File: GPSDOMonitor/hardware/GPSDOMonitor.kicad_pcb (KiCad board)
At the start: 2 copper layers, 4 parts, among them U1 PIC18LF2550-ISO, X1 ABM8W-20.0000MHZ-4-K1Z-T3

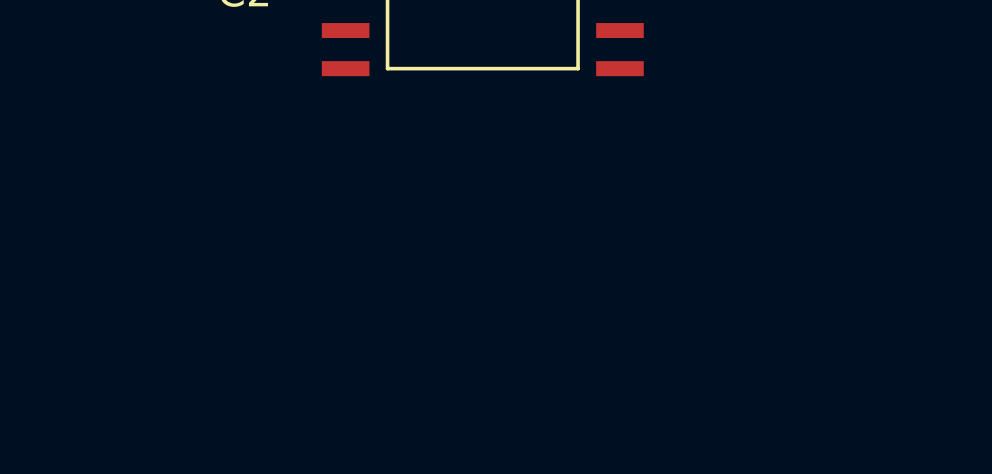
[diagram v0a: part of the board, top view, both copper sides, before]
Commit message: Add connector for the GPSDO
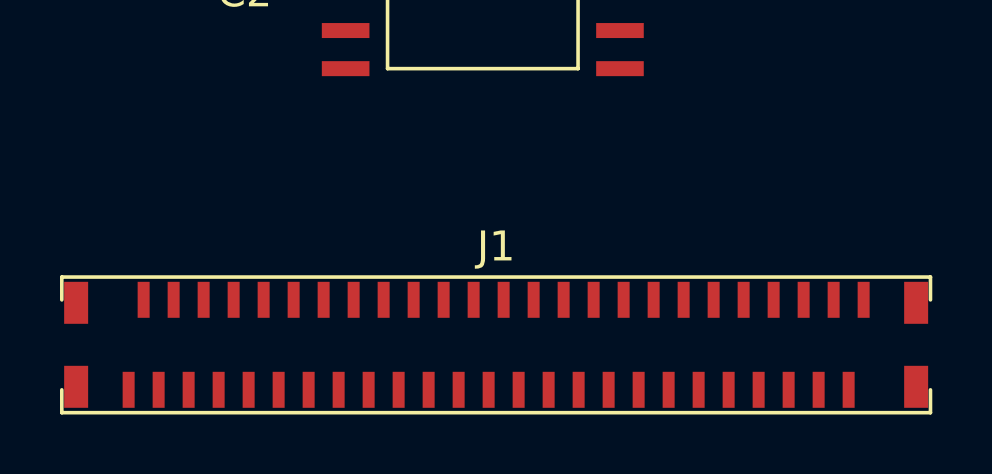
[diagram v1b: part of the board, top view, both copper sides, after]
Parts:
- added J1: F31S-1A7L1-11050, Connector_Data:F31S-1A7L1-11050, F.Cu at (96.1, 94.7)

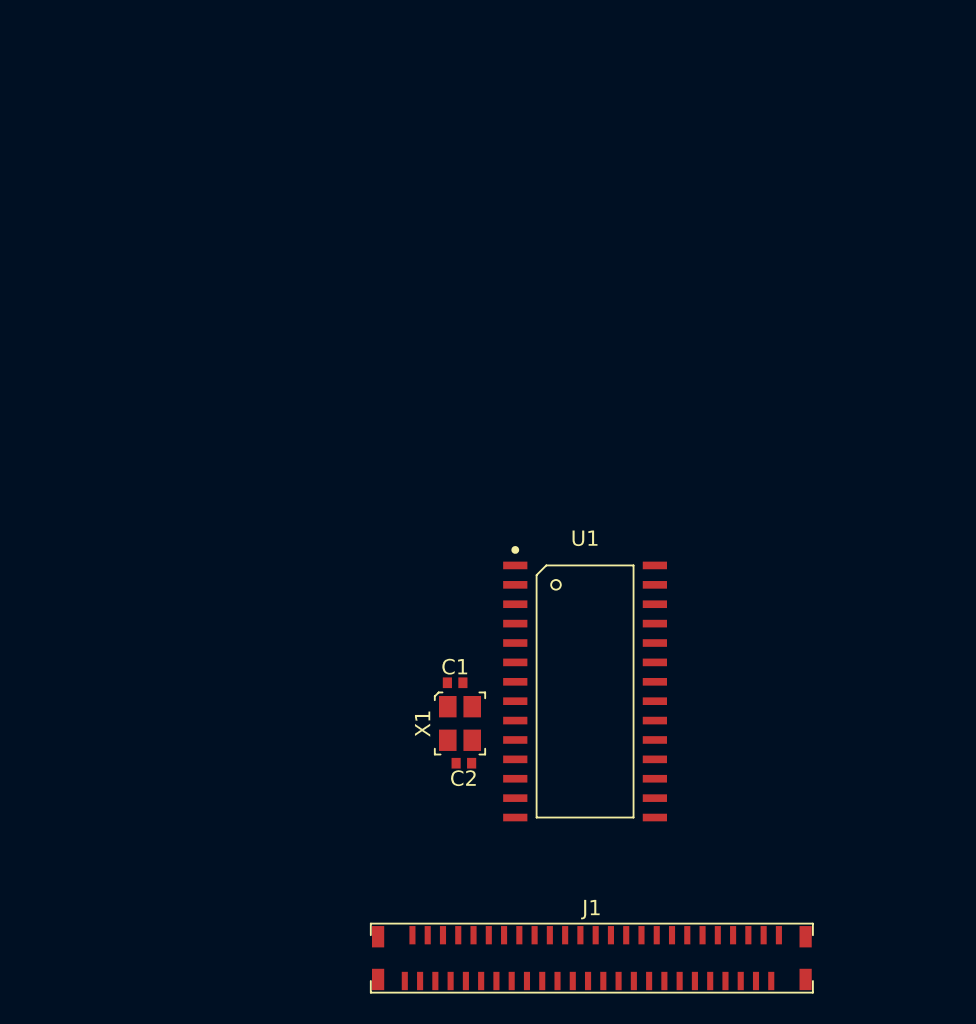
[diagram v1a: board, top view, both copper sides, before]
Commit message: Add 5.5v regulator schematic
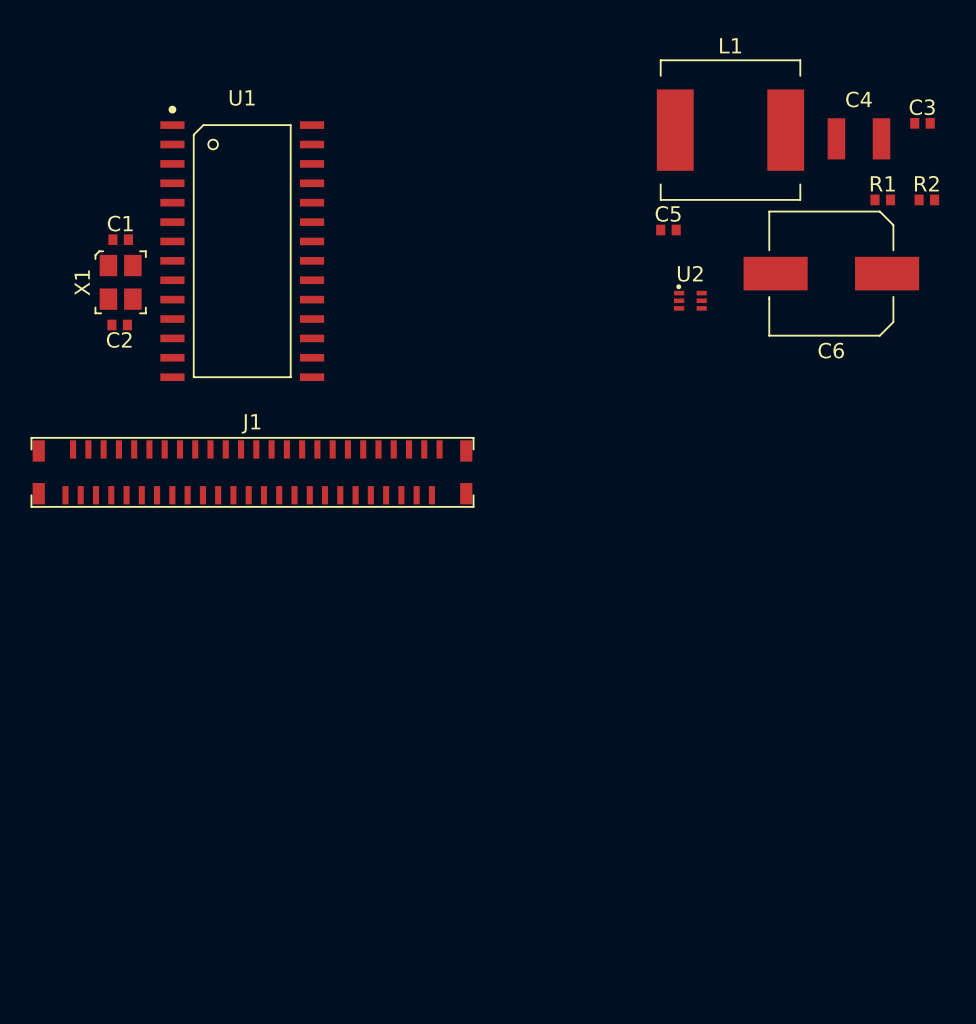
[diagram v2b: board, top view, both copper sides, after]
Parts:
- added C3: UMK105B7104KV-FR, Capacitor_Ceramic:C_0402_1005Metric, F.Cu at (117.7, 42.9)
- added C4: UMK325AB7106KM-P, Capacitor_Ceramic:C_1210_3225Metric, F.Cu at (113.6, 43.9)
- added C5: UMK105B7104KV-FR, Capacitor_Ceramic:C_0402_1005Metric, F.Cu at (101.1, 49.9)
- added C6: A768KE686M1GLAE038, Capacitor_Electrolytic:CP_Elec_KEMET_8mm, F.Cu at (111.8, 52.8)
- added L1: 74437356047, Inductor:74437356047, F.Cu at (105.2, 43.4)
- added R1: CRGCQ0402F82K, Resistor:R_0402_1005Metric, F.Cu at (115.1, 47.9)
- added R2: CRGCQ0402F10K, Resistor:R_0402_1005Metric, F.Cu at (118.0, 47.9)
- added U2: TPS563231DRLR, Package_TO_SOT:SOT-563, F.Cu at (102.5, 54.5)
- moved J1 38.8 mm to (73.9, 62.9)
- moved U1 36.5 mm to (73.2, 51.3)
- moved C2 36.5 mm to (65.2, 56.1)
- moved X1 36.5 mm to (65.2, 53.3)
- moved C1 36.4 mm to (65.2, 50.5)
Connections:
- net +5V renamed +5V5
- U1 pad 18: Net-(U1-Pad18) -> UART3_TxD
- U1 pad 25: Net-(U1-Pad25) -> UART4_TX

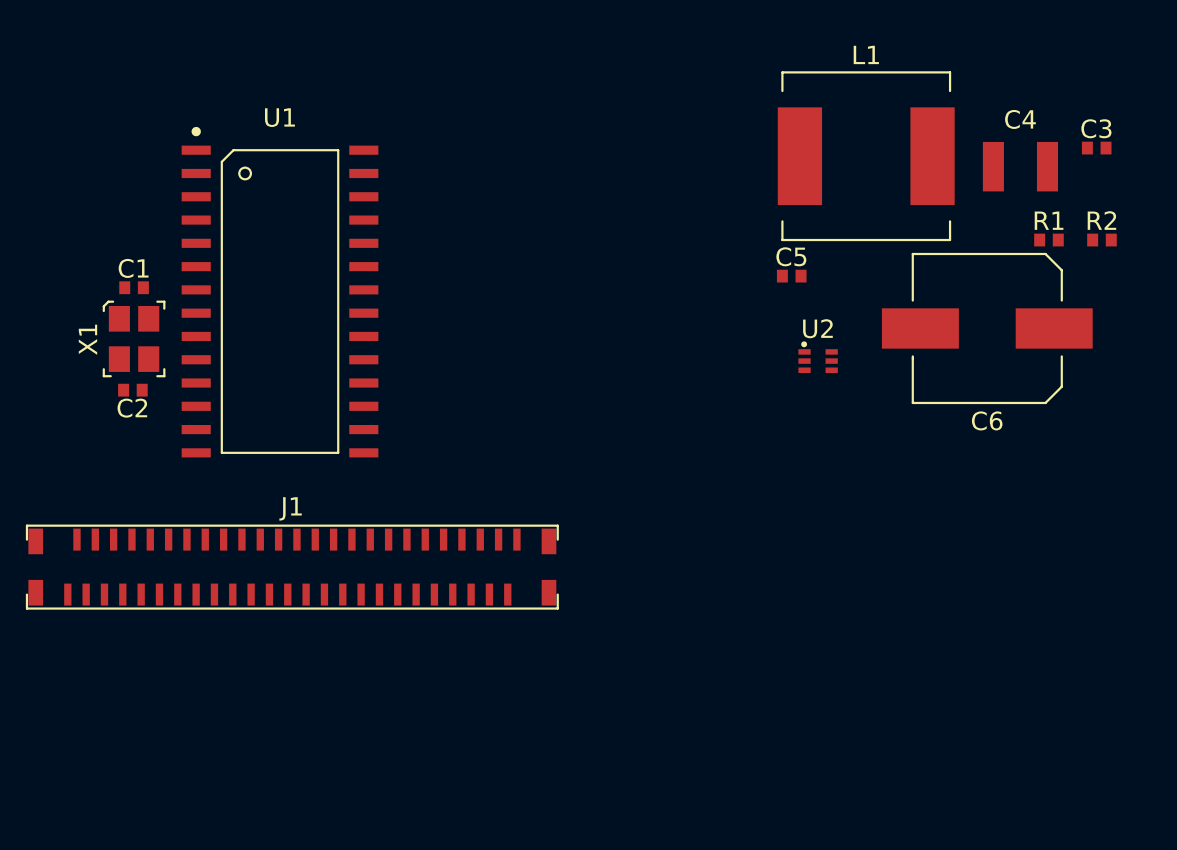
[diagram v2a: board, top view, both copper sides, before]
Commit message: Add 3.3v regulator for main CPU logic
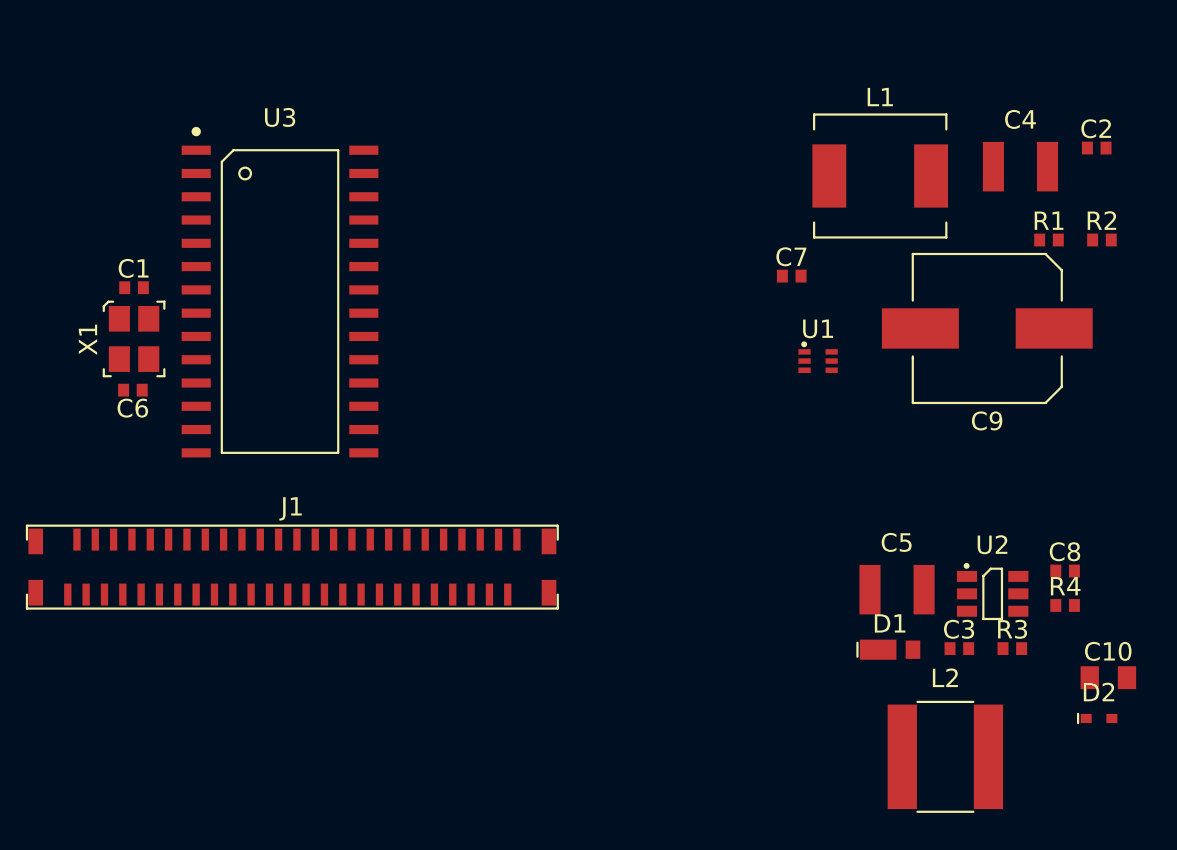
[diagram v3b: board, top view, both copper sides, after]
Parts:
- added C10: EMK212BB7106KG-T, Capacitor_Ceramic:C_0805_2012Metric, F.Cu at (118.4, 71.8)
- added C3: UMK105B7104KV-FR, Capacitor_Ceramic:C_0402_1005Metric, F.Cu at (110.2, 70.2)
- added C5: UMK325AB7106KM-P, Capacitor_Ceramic:C_1210_3225Metric, F.Cu at (106.8, 67.0)
- added C8: UMK105B7104KV-FR, Capacitor_Ceramic:C_0402_1005Metric, F.Cu at (116.0, 66.0)
- added D1: SS14HE, Diode:SOD-323HE, F.Cu at (106.5, 70.3)
- added D2: 1N914BWT, Diode:SOD-523, F.Cu at (117.9, 74.0)
- added L2: NR6028T150M, Inductor:NR6028, F.Cu at (109.5, 76.1)
- added R3: CRGCQ0402F33K, Resistor:R_0402_1005Metric, F.Cu at (113.1, 70.2)
- added R4: CRGCQ0402F10K, Resistor:R_0402_1005Metric, F.Cu at (116.0, 67.9)
- added U2: MCP16301T-I_CHY, Package_TO_SOT:SOT-23-6, F.Cu at (112.1, 67.2)
- L1: value 74437356047 -> ASPI-7318-4R7M-T; footprint Inductor:74437356047 -> Inductor:ASPI-7318
- moved L1 1.32 mm to (105.9, 44.5)
- renumbered C3 to C2, C2 to C6, C5 to C7, C6 to C9, U2 to U1, U1 to U3

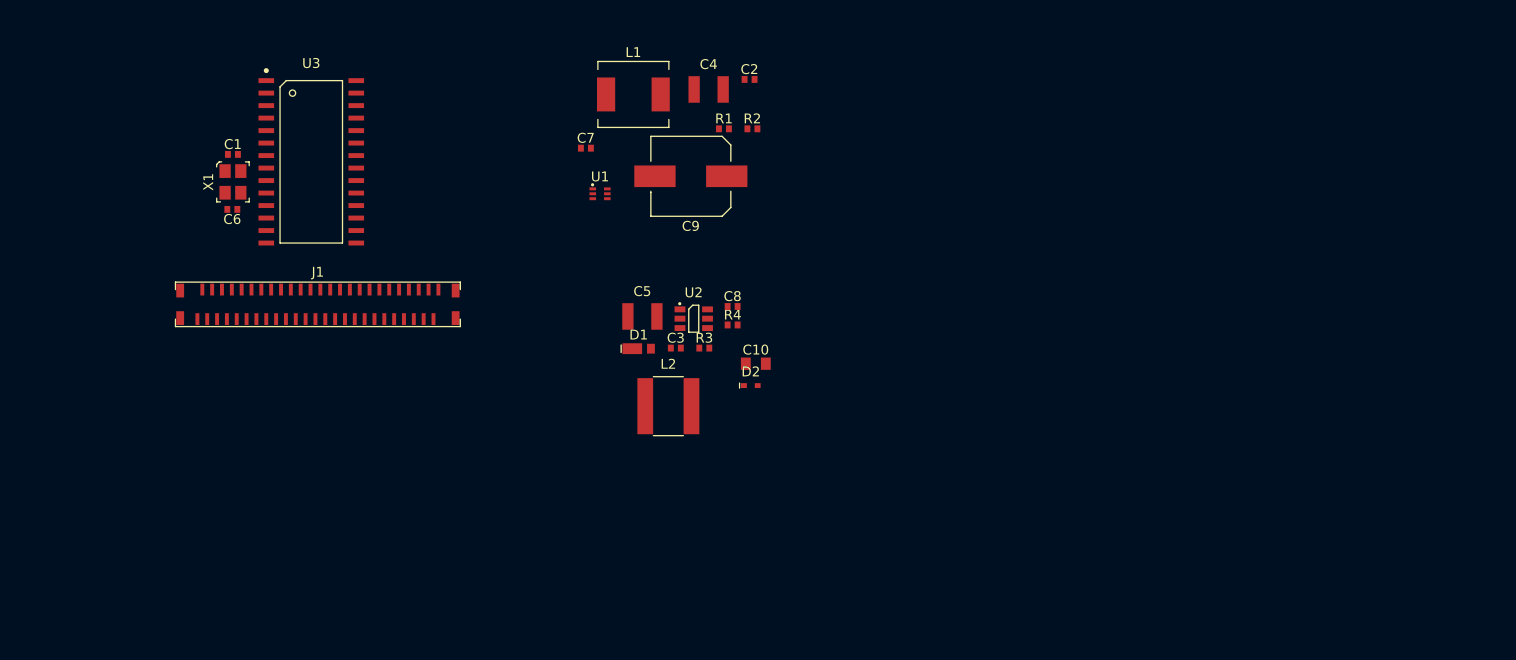
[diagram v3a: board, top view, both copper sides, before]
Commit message: Add shift registers for indication
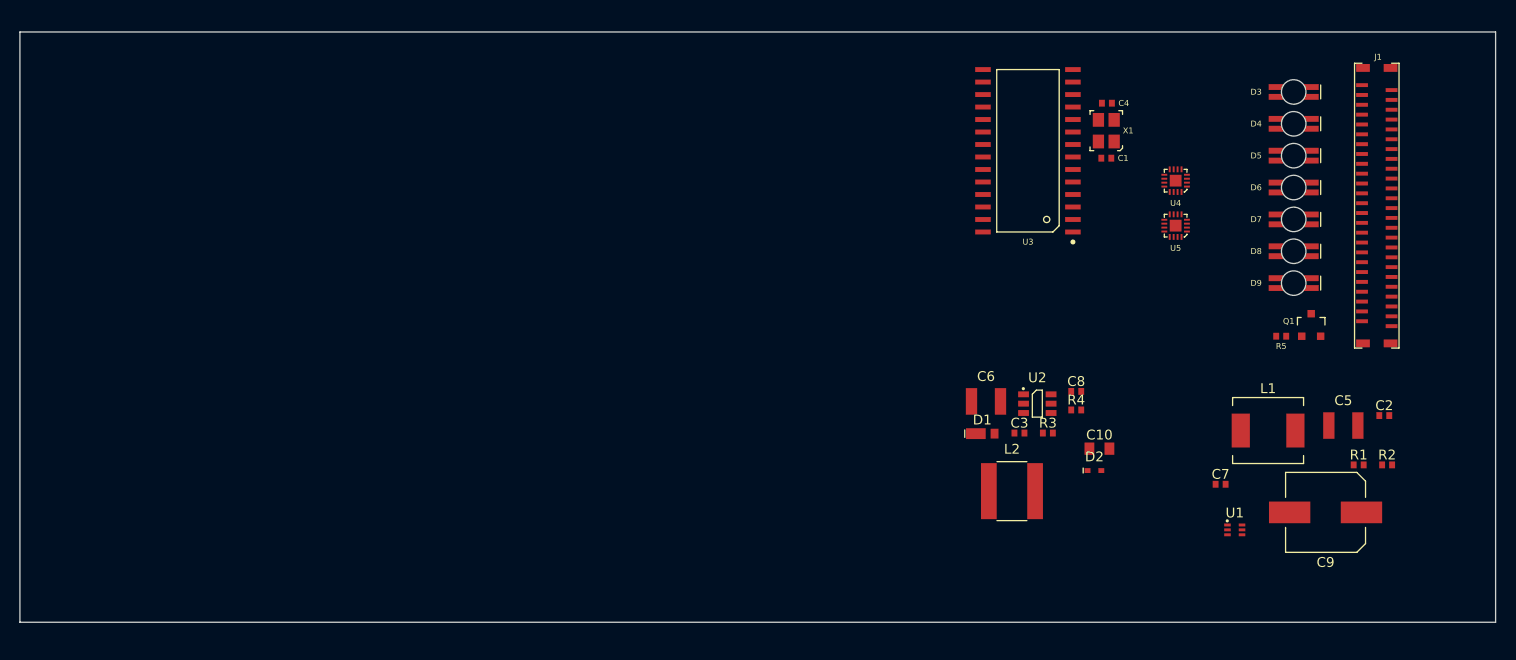
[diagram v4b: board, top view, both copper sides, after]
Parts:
- added D3: 5977703607F, LED:5977703607F, F.Cu at (173.0, 44.2)
- added D4: 5977703607F, LED:5977703607F, F.Cu at (173.0, 47.4)
- added D5: 5977703607F, LED:5977703607F, F.Cu at (173.0, 50.7)
- added D6: 5977703607F, LED:5977703607F, F.Cu at (173.0, 53.9)
- added D7: 5977703607F, LED:5977703607F, F.Cu at (173.0, 57.1)
- added D8: 5977703607F, LED:5977703607F, F.Cu at (173.0, 60.4)
- added D9: 5977703607F, LED:5977703607F, F.Cu at (173.0, 63.6)
- added Q1: MMBT3904LT1G, Package_TO_SOT:SOT-23, F.Cu at (174.8, 67.9)
- added R5: CRGCQ0402F1K0, Resistor:R_0402_1005Metric, F.Cu at (171.8, 69.0)
- added U4: SN74HC595BRWNR, Package_DFN_QFN:X1QFN-16_EP_2.5x2.5mm, F.Cu at (161.0, 53.2)
- added U5: SN74HC595BRWNR, Package_DFN_QFN:X1QFN-16_EP_2.5x2.5mm, F.Cu at (161.0, 57.8)
- moved J1 110.8 mm to (184.4, 55.8), turned to 270 degrees
- moved C4 89.6 mm to (154.1, 45.3), turned to 0 degrees
- moved X1 88.9 mm to (154.0, 48.1), turned to 90 degrees
- moved C1 88.8 mm to (154.0, 50.9), turned to 180 degrees
- moved C5 73.0 mm to (178.1, 78.1)
- moved R1 73.0 mm to (179.6, 82.1)
- moved U1 73.0 mm to (167.0, 88.7)
- moved C2 73.0 mm to (182.2, 77.1)
- moved C7 73.0 mm to (165.6, 84.1)
- moved C9 73.0 mm to (176.3, 86.9)
- moved L1 73.0 mm to (170.4, 78.6)
- moved R2 73.0 mm to (182.5, 82.1)
- moved U3 72.9 mm to (146.0, 50.2), turned to 180 degrees
- moved C8 36.0 mm to (150.9, 74.6)
- moved D2 36.0 mm to (152.8, 82.7)
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- renumbered C6 to C4, C4 to C5, C5 to C6
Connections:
- U3 pad 13: Net-(U3-Pad13) -> /LED_PWM
- U3 pad 3: Net-(U3-Pad3) -> /SER
- U3 pad 4: Net-(U3-Pad4) -> /OE
- U3 pad 5: Net-(U3-Pad5) -> /RCLK
- U3 pad 6: Net-(U3-Pad6) -> /SRCLK
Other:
- board outline added: 150 x 60 mm

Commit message: Route power supplies
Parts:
- removed the R3 at (148.1, 78.9)
- added R1: CRG0402ZR, Resistor:R_0402_1005Metric, F.Cu at (160.8, 86.0)
- added R4: CRGCQ0402F33K, Resistor:R_0402_1005Metric, F.Cu at (158.9, 81.8)
- moved D1 24.6 mm to (165.9, 81.8)
- moved C6 24.5 mm to (163.6, 86.7)
- moved L2 20.6 mm to (163.4, 77.0), turned to 90 degrees
- moved C3 20.5 mm to (165.1, 83.8), turned to 270 degrees
- moved U2 16.4 mm to (161.5, 83.3)
- moved C10 15.0 mm to (167.5, 75.7), turned to 270 degrees
- moved C9 12.5 mm to (183.4, 76.7)
- moved C7 12.4 mm to (176.3, 77.7)
- moved U1 12.0 mm to (175.0, 79.8), turned to 90 degrees
- moved C8 11.6 mm to (160.7, 81.0)
- moved R5 10.8 mm to (158.9, 83.8), turned to 90 degrees
- moved L1 10.2 mm to (178.6, 84.7)
- moved R3 9.77 mm to (173.4, 78.7), turned to 270 degrees
- moved C2 9.62 mm to (173.4, 80.8), turned to 90 degrees
- moved R2 8.29 mm to (173.4, 76.7), turned to 270 degrees
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- renumbered R1 to R2, R2 to R3, R4 to R5, R5 to R6
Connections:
- U2 pad 4: +12V -> Net-(R1-Pad2)
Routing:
- net +5V5: track 0.00 -> 15.6 mm
- net +3V3: track 0.00 -> 14.6 mm
- net +12V: track 0.00 -> 13.1 mm
- net GND: track 0.00 -> 11.7 mm
- net Net-(R4-Pad2): track 0.00 -> 4.91 mm
- net Net-(C7-Pad2): track 0.00 -> 4.54 mm
- net Net-(R2-Pad2): track 0.00 -> 3.08 mm
- net Net-(C8-Pad1): track 0.00 -> 2.77 mm
- net Net-(R1-Pad2): track 0.00 -> 2.66 mm
- net Net-(C7-Pad1): track 0.00 -> 1.40 mm
- added copper zone on F.Cu, net +5V5
- added copper zone on F.Cu, net GND
- added copper zone on F.Cu, net Net-(C8-Pad2)
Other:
- net class Default: clearance 0.2 -> 0.1; trace_width 0.25 -> 0.1524; via_dia 0.8 -> 0.508; via_drill 0.4 -> 0.3048
- rule pad_to_mask_clearance: 0 -> 0.05
- rule trace_clearance: 0.2 -> 0.1
- rule trace_min: 0.2 -> 0.1524
- rule via_min_drill: 0.3 -> 0.1524
- rule via_min_size: 0.4 -> 0.1524
